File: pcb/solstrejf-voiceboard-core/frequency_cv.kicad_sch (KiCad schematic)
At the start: 23 parts, among them U5 LM324, U7 L78L12, U8 L79L12

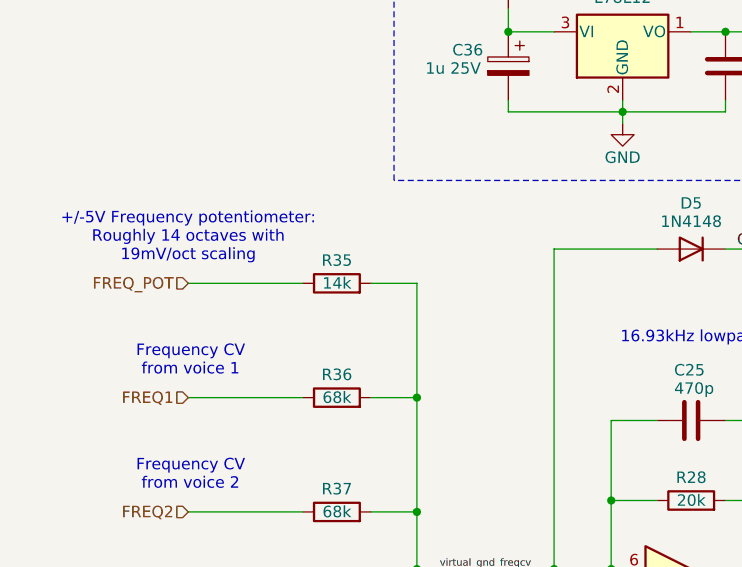
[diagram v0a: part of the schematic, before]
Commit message: Updated resistor value in VCF CV circuit. Generated new ibom and schematic.
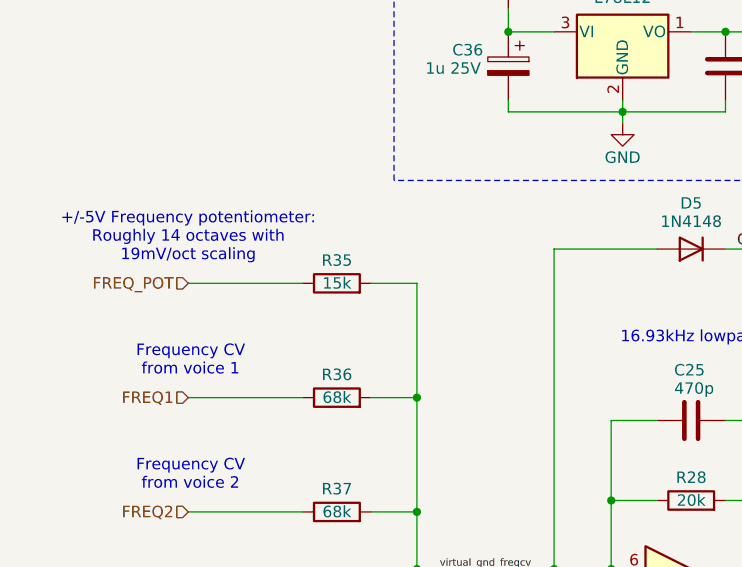
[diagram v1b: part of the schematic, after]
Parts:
- R35: value 14k -> 15k
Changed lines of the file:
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@@
 	(title_block
 		(title "Frequency Control Voltage Summing Amplifier")
-		(date "2025-03-01")
+		(date "2025-03-02")
 		(rev "1.1")
 	)
@@
 			)
 		)
-		(property "Value" "14k"
+		(property "Value" "15k"
 			(at 92.71 67.31 90)
 			(effects
